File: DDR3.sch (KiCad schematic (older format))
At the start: 59 parts, among them U15 MT41K256M16HA-125_E, U16 MT41K256M16HA-125_E, U20 xc7z020clg484, U8 TPS51200DRCR

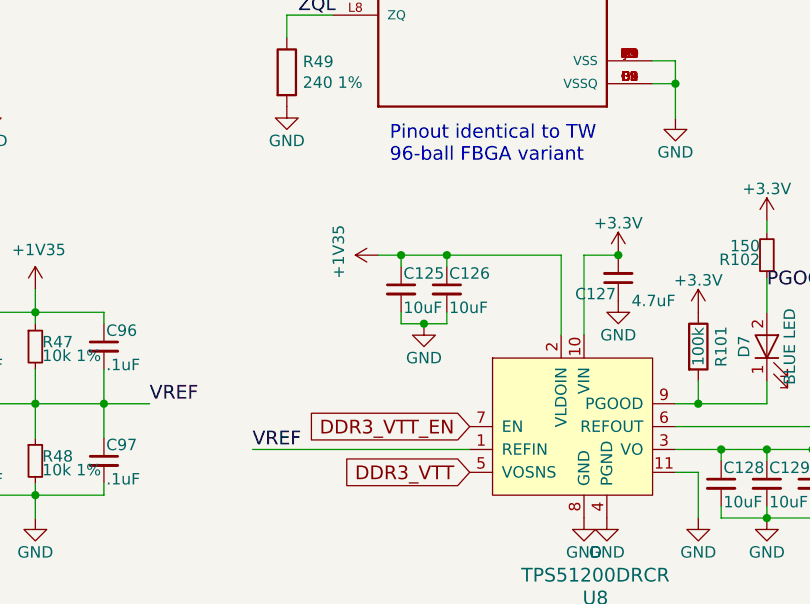
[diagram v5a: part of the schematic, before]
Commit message: routed a few things, about to remove power jack and 5V regulator
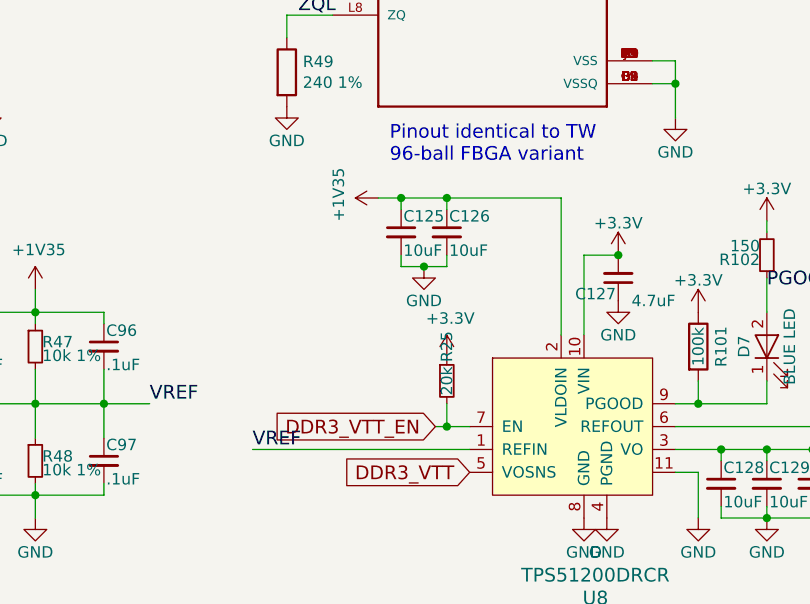
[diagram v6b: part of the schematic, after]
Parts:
- added R25: 20k, Resistor_SMD:R_0402_1005Metric, symbol Device:R_Small
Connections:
- net +3V3: now also R25.1
- net DDR3_VTT_EN: now also R25.2
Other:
- moved on the sheet: C125, C126
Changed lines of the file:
@@
 	3750 7300 4700 7300
 Wire Wire Line
-	4600 6450 5100 6450
-Connection ~ 4600 6450
+	4600 6200 5100 6200
+Connection ~ 4600 6200
+Wire Wire Line
+	4600 6250 4600 6200
+Wire Wire Line
+	4400 6200 4600 6200
+Connection ~ 4400 6200
+Wire Wire Line
+	4400 6250 4400 6200
 Wire Wire Line
 	4600 6500 4600 6450
 Wire Wire Line
-	4400 6450 4600 6450
-Connection ~ 4400 6450
-Wire Wire Line
-	4400 6500 4400 6450
-Wire Wire Line
-	4600 6750 4600 6700
-Wire Wire Line
-	4300 6450 4400 6450
-Wire Wire Line
-	5100 6450 5100 6800
+	4300 6200 4400 6200
 Text Label 3750 7300 0    60   ~ 0
 VREF
-Text GLabel 4700 7200 0    60   Input ~ 0
+Text GLabel 4550 7200 0    60   Input ~ 0
 DDR3_VTT_EN
 Connection ~ 5700 7100
@@
 $EndComp
 Wire Wire Line
-	4500 6750 4600 6750
-Connection ~ 4500 6750
+	4500 6500 4600 6500
+Connection ~ 4500 6500
 $Comp
 L power:GND #PWR072
 U 1 1 5CDB5416
-P 4500 6750
-F 0 "#PWR072" H 4500 6500 50  0001 C CNN
-F 1 "GND" H 4500 6600 50  0000 C CNN
-F 2 "" H 4500 6750 50  0000 C CNN
-F 3 "" H 4500 6750 50  0000 C CNN
-	1    4500 6750
-	1    0    0    -1
-$EndComp
-Wire Wire Line
-	4400 6750 4500 6750
-Wire Wire Line
-	4400 6700 4400 6750
+P 4500 6500
+F 0 "#PWR072" H 4500 6250 50  0001 C CNN
+F 1 "GND" H 4500 6350 50  0000 C CNN
+F 2 "" H 4500 6500 50  0000 C CNN
+F 3 "" H 4500 6500 50  0000 C CNN
+	1    4500 6500
+	1    0    0    -1
+$EndComp
+Wire Wire Line
+	4400 6500 4500 6500
+Wire Wire Line
+	4400 6450 4400 6500
 $Comp
 L Device:C_Small C?
 U 1 1 5CD9C840
-P 4600 6600
+P 4600 6350
 AR Path="/58508414/5CD9C840" Ref="C?"  Part="1"
 AR Path="/58818A06/5CD9C840" Ref="C126"  Part="1"
-F 0 "C126" H 4610 6670 50  0000 L CNN
-F 1 "10uF" H 4610 6520 50  0000 L CNN
-F 2 "Capacitor_SMD:C_0603_1608Metric" H 4600 6600 50  0001 C CNN
-F 3 "" H 4600 6600 50  0001 C CNN
-F 4 "Murata" H 1000 3650 50  0001 C CNN "MFR"
-F 5 "GRM21BR61A106KE19L" H 1000 3650 50  0001 C CNN "MPN"
-F 6 "Digikey" H 1000 3650 50  0001 C CNN "SPR"
-F 7 "490-1709-1-ND" H 1000 3650 50  0001 C CNN "SPN"
-F 8 "" H 1000 3650 50  0001 C CNN "SPURL"
-	1    4600 6600
+F 0 "C126" H 4610 6420 50  0000 L CNN
+F 1 "10uF" H 4610 6270 50  0000 L CNN
+F 2 "Capacitor_SMD:C_0603_1608Metric" H 4600 6350 50  0001 C CNN
+F 3 "" H 4600 6350 50  0001 C CNN
+F 4 "Murata" H 1000 3400 50  0001 C CNN "MFR"
+F 5 "GRM21BR61A106KE19L" H 1000 3400 50  0001 C CNN "MPN"
+F 6 "Digikey" H 1000 3400 50  0001 C CNN "SPR"
+F 7 "490-1709-1-ND" H 1000 3400 50  0001 C CNN "SPN"
+F 8 "" H 1000 3400 50  0001 C CNN "SPURL"
+	1    4600 6350
 	1    0    0    -1
 $EndComp
@@
 L Device:C_Small C?
 U 1 1 5CD9C834
-P 4400 6600
+P 4400 6350
 AR Path="/58508414/5CD9C834" Ref="C?"  Part="1"
 AR Path="/58818A06/5CD9C834" Ref="C125"  Part="1"
-F 0 "C125" H 4410 6670 50  0000 L CNN
-F 1 "10uF" H 4410 6520 50  0000 L CNN
-F 2 "Capacitor_SMD:C_0603_1608Metric" H 4400 6600 50  0001 C CNN
-F 3 "" H 4400 6600 50  0001 C CNN
-F 4 "Murata" H 800 3650 50  0001 C CNN "MFR"
-F 5 "GRM21BR61A106KE19L" H 800 3650 50  0001 C CNN "MPN"
-F 6 "Digikey" H 800 3650 50  0001 C CNN "SPR"
-F 7 "490-1709-1-ND" H 800 3650 50  0001 C CNN "SPN"
-F 8 "" H 800 3650 50  0001 C CNN "SPURL"
-	1    4400 6600
+F 0 "C125" H 4410 6420 50  0000 L CNN
+F 1 "10uF" H 4410 6270 50  0000 L CNN
+F 2 "Capacitor_SMD:C_0603_1608Metric" H 4400 6350 50  0001 C CNN
+F 3 "" H 4400 6350 50  0001 C CNN
+F 4 "Murata" H 800 3400 50  0001 C CNN "MFR"
+F 5 "GRM21BR61A106KE19L" H 800 3400 50  0001 C CNN "MPN"
+F 6 "Digikey" H 800 3400 50  0001 C CNN "SPR"
+F 7 "490-1709-1-ND" H 800 3400 50  0001 C CNN "SPN"
+F 8 "" H 800 3400 50  0001 C CNN "SPURL"
+	1    4400 6350
 	1    0    0    -1
 $EndComp
@@
 L power:+1V35 #PWR060
 U 1 1 5CD61F44
-P 4300 6450
-F 0 "#PWR060" H 4300 6300 50  0001 C CNN
-F 1 "+1V35" H 4315 6623 50  0000 C CNN
-F 2 "" H 4300 6450 50  0001 C CNN
-F 3 "" H 4300 6450 50  0001 C CNN
-	1    4300 6450
+P 4300 6200
+F 0 "#PWR060" H 4300 6050 50  0001 C CNN
+F 1 "+1V35" H 4315 6373 50  0000 C CNN
+F 2 "" H 4300 6200 50  0001 C CNN
+F 3 "" H 4300 6200 50  0001 C CNN
+	1    4300 6200
 	0    -1   -1   0
 $EndComp
@@
 	1    0    0    -1
 $EndComp
+Wire Wire Line
+	5100 6200 5100 6800
+$Comp
+L Device:R_Small R?
+U 1 1 5DDFD56F
+P 4600 7000
+AR Path="/5852A88E/5DDFD56F" Ref="R?"  Part="1"
+AR Path="/5CA1ABAE/5DDFD56F" Ref="R?"  Part="1"
+AR Path="/58818A06/5DDFD56F" Ref="R25"  Part="1"
+F 0 "R25" V 4600 7150 50  0000 C CNN
+F 1 "20k" V 4600 7000 50  0000 C CNN
+F 2 "Resistor_SMD:R_0402_1005Metric" H 4600 7000 50  0001 C CNN
+F 3 "" H 4600 7000 50  0001 C CNN
+	1    4600 7000
+	1    0    0    -1
+$EndComp
+Wire Wire Line
+	4700 7200 4600 7200
+Wire Wire Line
+	4600 7100 4600 7200
+Connection ~ 4600 7200
+Wire Wire Line
+	4600 7200 4550 7200
+$Comp
+L power:+3V3 #PWR?
+U 1 1 5DE96F1D
+P 4600 6900
+AR Path="/5852A88E/5DE96F1D" Ref="#PWR?"  Part="1"
+AR Path="/5CA1ABAE/5DE96F1D" Ref="#PWR?"  Part="1"
+AR Path="/58818A06/5DE96F1D" Ref="#PWR0176"  Part="1"
+F 0 "#PWR0176" H 4600 6750 50  0001 C CNN
+F 1 "+3.3V" H 4615 7073 50  0000 C CNN
+F 2 "" H 4600 6900 50  0001 C CNN
+F 3 "" H 4600 6900 50  0001 C CNN
+	1    4600 6900
+	1    0    0    -1
+$EndComp

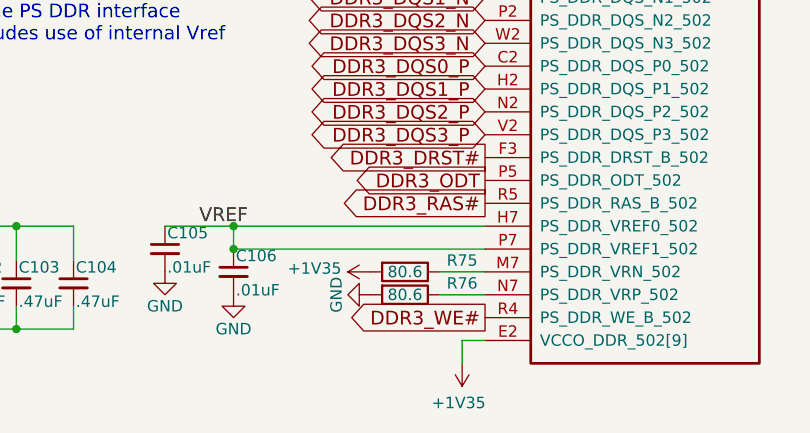
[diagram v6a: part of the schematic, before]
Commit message: length matched important interfaces, added current sense resistors to regulators, about to shrink silkscreen designators
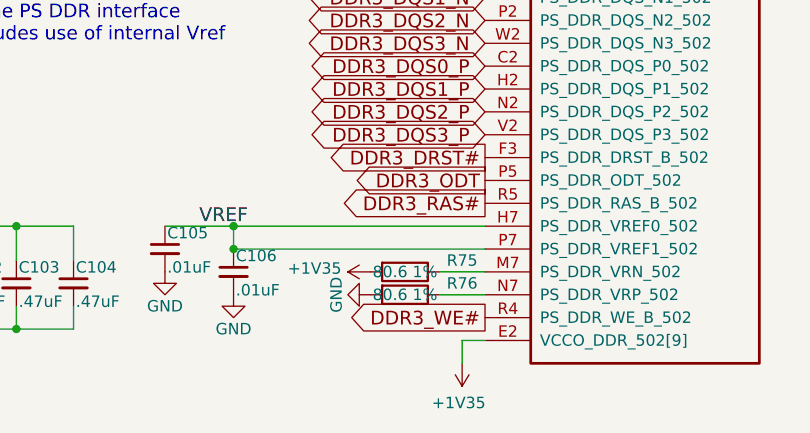
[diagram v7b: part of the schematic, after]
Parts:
- C105, C106, C93, C98: MPN (none) -> GRM155R71H103KA88J; SPN (none) -> 490-6351-1-ND; SPURL (none) -> -
- R25: MFR (none) -> Yageo; MPN (none) -> RT0402BRD0720KL; SPN (none) -> YAG1388CT-ND; SPR (none) -> Digikey; SPURL (none) -> -
- R46, R49: MFR (none) -> Yageo; MPN (none) -> RC0402FR-07240RL; SPN (none) -> 311-240LRTR-ND; SPR (none) -> Digikey; SPURL (none) -> -
- R47, R48: MPN (none) -> RC0402FR-0710KL; SPN (none) -> 311-10.0KLRCT-ND; SPURL (none) -> -
- R50: MPN (none) -> RC0402FR-0780R6L; SPN (none) -> 311-80.6LRTR-ND; SPURL (none) -> -
- R51, R52, R53, R54, R55, R56, R57, R58, R59, R60, R61, R62, R63, R64, R65, R66, R67, R68, R69, R70, R71, R72, R73: MFR (none) -> Yageo; MPN (none) -> RC0402FR-0740R2L; SPN (none) -> 311-40.2LRTR-ND; SPR (none) -> Digikey; SPURL (none) -> -
- R74: MFR (none) -> Yageo; MPN (none) -> RC0402JR-074K7L; SPN (none) -> 311-4.7KJRCT-ND; SPR (none) -> Digikey; SPURL (none) -> -
- R75, R76: value 80.6 -> 80.6 1%; MFR (none) -> Yageo; MPN (none) -> RC0402FR-0780R6L; SPN (none) -> 311-80.6LRTR-ND; SPR (none) -> Digikey; SPURL (none) -> -
- U15, U16: MFR (none) -> Micron; MPN (none) -> MT41K256M16HA-125:E; SPN (none) -> MT41K256M16HA-125:E-ND; SPR (none) -> Digikey; SPURL (none) -> -
- U20: MFR (none) -> Xilinx; MPN (none) -> XC7Z020-1CLG484C; SPN (none) -> 122-1850-ND; SPR (none) -> Digikey; SPURL (none) -> -
- U8: MFR (none) -> Texas Instruments; SPN (none) -> 296-26978-1-ND; SPR (none) -> Digikey; SPURL (none) -> -

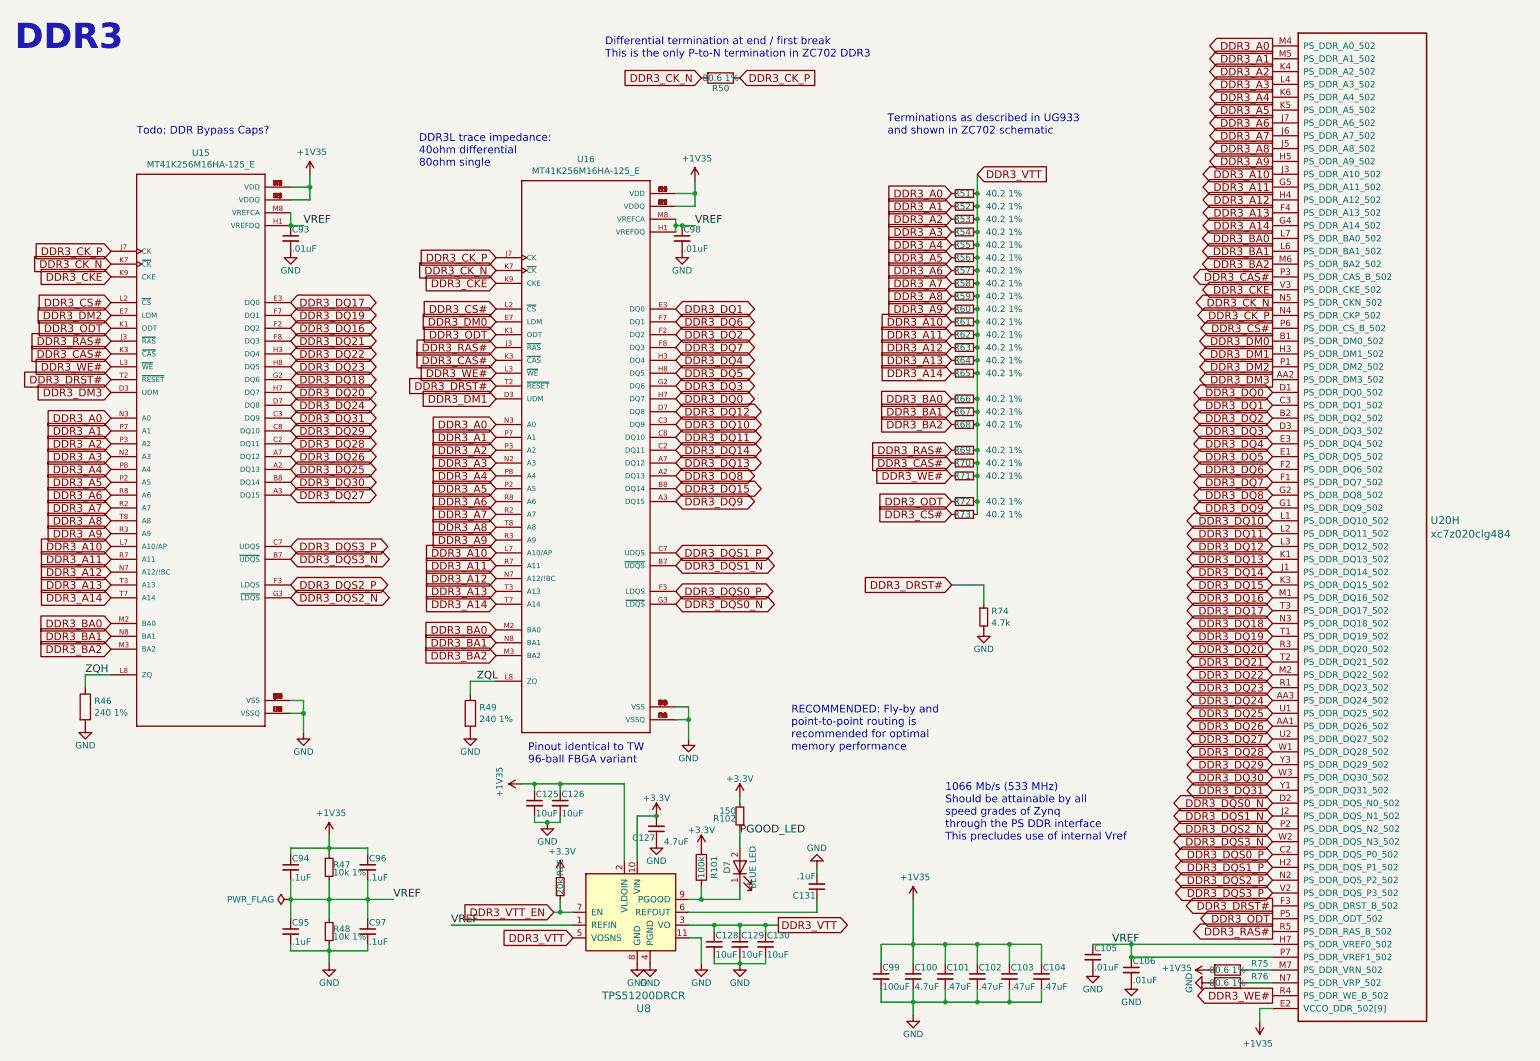
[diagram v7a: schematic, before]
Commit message: finished review with gerber output. still need to relocate rangefinders / LEDs
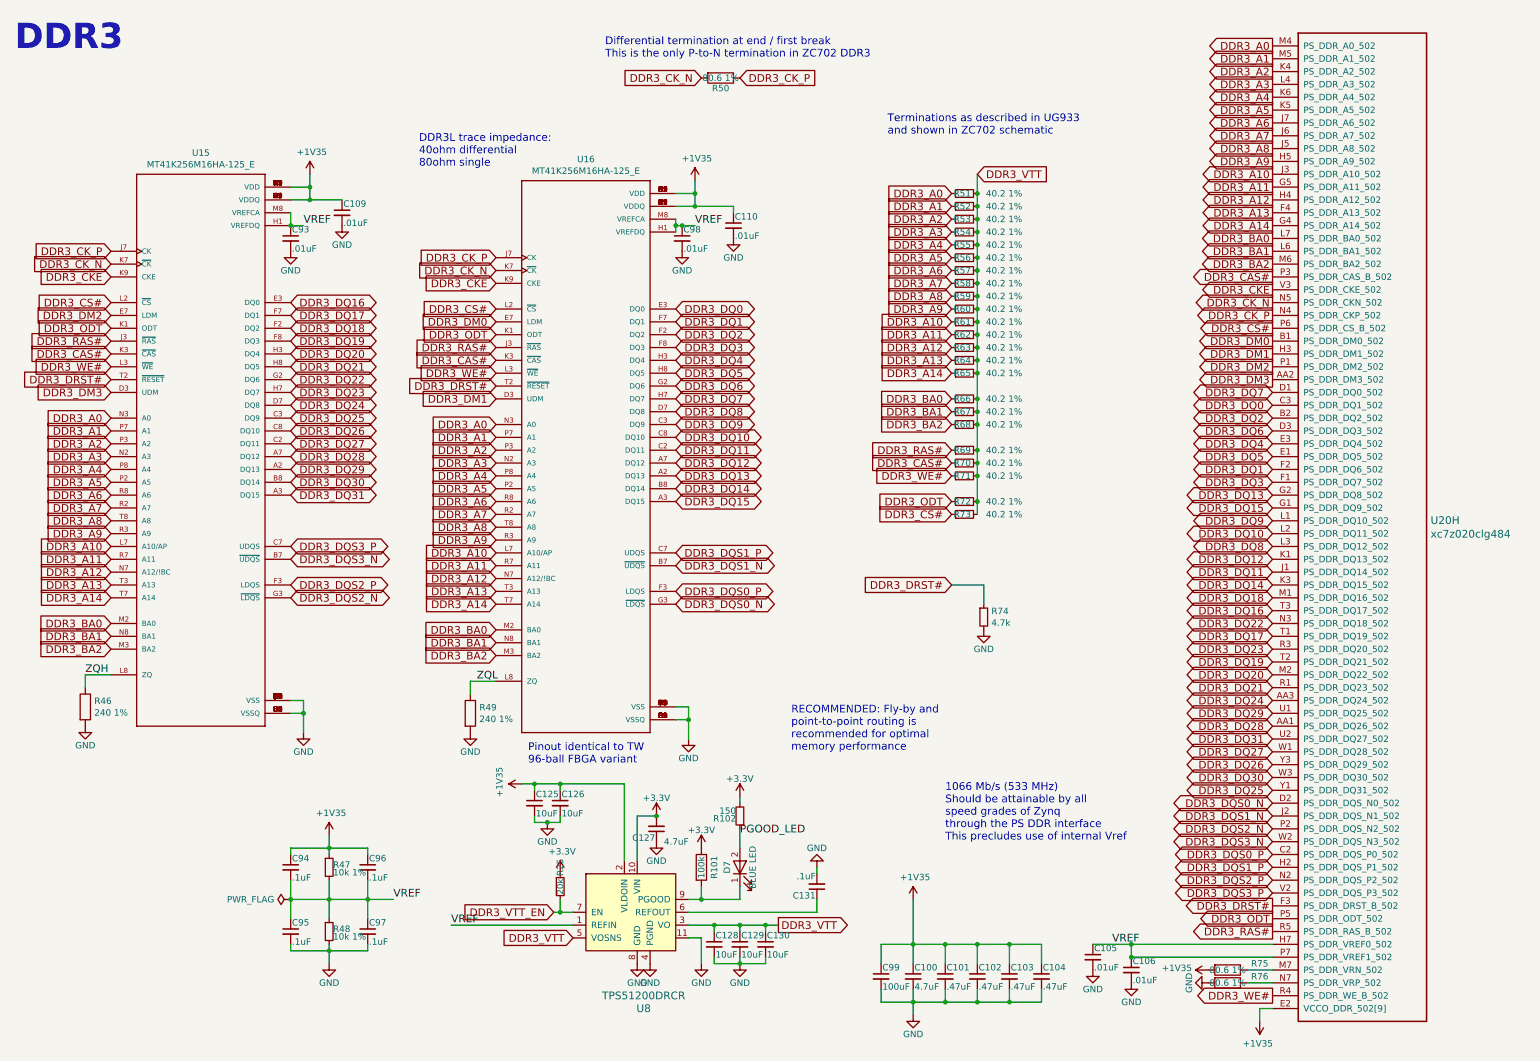
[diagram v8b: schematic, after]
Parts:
- added C109, C110: .01uF, Capacitor_SMD:C_0402_1005Metric, symbol Device:C_Small
- U15, U16: MPN MT41K256M16HA-125:E -> MT41K256M16TW-107; SPN MT41K256M16HA-125:E-ND -> 557-2006-6-ND
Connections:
- net +1V35: now also C109.1, C110.1
- net DDR3_DQ0: now also U16.E3 (DQ0), U20.C3 (PS_DDR_DQ1_502); no longer U16.H7 (DQ7), U20.D1 (PS_DDR_DQ0_502)
- net DDR3_DQ1: now also U16.F7 (DQ1), U20.F2 (PS_DDR_DQ6_502); no longer U16.E3 (DQ0), U20.C3 (PS_DDR_DQ1_502)
- net DDR3_DQ10: now also U16.C8 (DQ10), U20.L2 (PS_DDR_DQ11_502); no longer U16.C3 (DQ9), U20.L1 (PS_DDR_DQ10_502)
- net DDR3_DQ11: now also U16.C2 (DQ11), U20.J1 (PS_DDR_DQ14_502); no longer U16.C8 (DQ10), U20.L2 (PS_DDR_DQ11_502)
- net DDR3_DQ12: now also U16.A7 (DQ12), U20.K1 (PS_DDR_DQ13_502); no longer U16.D7 (DQ8), U20.L3 (PS_DDR_DQ12_502)
- net DDR3_DQ13: now also U16.A2 (DQ13), U20.G2 (PS_DDR_DQ8_502); no longer U16.A7 (DQ12), U20.K1 (PS_DDR_DQ13_502)
- net DDR3_DQ14: now also U16.B8 (DQ14), U20.K3 (PS_DDR_DQ15_502); no longer U16.C2 (DQ11), U20.J1 (PS_DDR_DQ14_502)
- net DDR3_DQ15: now also U16.A3 (DQ15), U20.G1 (PS_DDR_DQ9_502); no longer U16.B8 (DQ14), U20.K3 (PS_DDR_DQ15_502)
- net DDR3_DQ16: now also U15.E3 (DQ0), U20.T3 (PS_DDR_DQ17_502); no longer U15.F2 (DQ2), U20.M1 (PS_DDR_DQ16_502)
- net DDR3_DQ17: now also U15.F7 (DQ1), U20.T1 (PS_DDR_DQ19_502); no longer U15.E3 (DQ0), U20.T3 (PS_DDR_DQ17_502)
- net DDR3_DQ18: now also U15.F2 (DQ2), U20.M1 (PS_DDR_DQ16_502); no longer U15.G2 (DQ6), U20.N3 (PS_DDR_DQ18_502)
- net DDR3_DQ19: now also U15.F8 (DQ3), U20.T2 (PS_DDR_DQ21_502); no longer U15.F7 (DQ1), U20.T1 (PS_DDR_DQ19_502)
- net DDR3_DQ20: now also U15.H3 (DQ4), U20.M2 (PS_DDR_DQ22_502); no longer U15.H7 (DQ7), U20.R3 (PS_DDR_DQ20_502)
- net DDR3_DQ21: now also U15.H8 (DQ5), U20.R1 (PS_DDR_DQ23_502); no longer U15.F8 (DQ3), U20.T2 (PS_DDR_DQ21_502)
- net DDR3_DQ22: now also U15.G2 (DQ6), U20.N3 (PS_DDR_DQ18_502); no longer U15.H3 (DQ4), U20.M2 (PS_DDR_DQ22_502)
- net DDR3_DQ23: now also U15.H7 (DQ7), U20.R3 (PS_DDR_DQ20_502); no longer U15.H8 (DQ5), U20.R1 (PS_DDR_DQ23_502)
- net DDR3_DQ25: now also U15.C3 (DQ9), U20.Y1 (PS_DDR_DQ31_502); no longer U15.A2 (DQ13), U20.U1 (PS_DDR_DQ25_502)
- net DDR3_DQ26: now also U15.C8 (DQ10), U20.Y3 (PS_DDR_DQ29_502); no longer U15.A7 (DQ12), U20.AA1 (PS_DDR_DQ26_502)
- net DDR3_DQ27: now also U15.C2 (DQ11), U20.W1 (PS_DDR_DQ28_502); no longer U15.A3 (DQ15), U20.U2 (PS_DDR_DQ27_502)
- net DDR3_DQ28: now also U15.A7 (DQ12), U20.AA1 (PS_DDR_DQ26_502); no longer U15.C2 (DQ11), U20.W1 (PS_DDR_DQ28_502)
- net DDR3_DQ29: now also U15.A2 (DQ13), U20.U1 (PS_DDR_DQ25_502); no longer U15.C8 (DQ10), U20.Y3 (PS_DDR_DQ29_502)
- net DDR3_DQ3: now also U16.F8 (DQ3), U20.F1 (PS_DDR_DQ7_502); no longer U16.G2 (DQ6), U20.D3 (PS_DDR_DQ3_502)
- net DDR3_DQ31: now also U15.A3 (DQ15), U20.U2 (PS_DDR_DQ27_502); no longer U15.C3 (DQ9), U20.Y1 (PS_DDR_DQ31_502)
- net DDR3_DQ6: now also U16.G2 (DQ6), U20.D3 (PS_DDR_DQ3_502); no longer U16.F7 (DQ1), U20.F2 (PS_DDR_DQ6_502)
- net DDR3_DQ7: now also U16.H7 (DQ7), U20.D1 (PS_DDR_DQ0_502); no longer U16.F8 (DQ3), U20.F1 (PS_DDR_DQ7_502)
- net DDR3_DQ8: now also U16.D7 (DQ8), U20.L3 (PS_DDR_DQ12_502); no longer U16.A2 (DQ13), U20.G2 (PS_DDR_DQ8_502)
- net DDR3_DQ9: now also U16.C3 (DQ9), U20.L1 (PS_DDR_DQ10_502); no longer U16.A3 (DQ15), U20.G1 (PS_DDR_DQ9_502)
- net GND: now also C109.2, C110.2
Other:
- note removed: "Todo: DDR Bypass Caps?"
